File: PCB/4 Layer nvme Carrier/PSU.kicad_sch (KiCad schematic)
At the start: 176 parts, among them J481 Conn_01x02_Pin, J5 Barrel_Jack_Switch, J79 Conn_01x02_Pin, J80 Conn_01x02_Pin, J82 Conn_01x04, Q8 2N7002, SW1 SW_Push, SW2 SW_Push, U15 SY8253ADC, U16 SY8253ADC, U400 SY8253ADC, U410 SY8253ADC, U420 SY8253ADC, U430 SY8253ADC, U440 SY8253ADC, U450 SY8253ADC, U460 SY8253ADC, U470 SY8253ADC, U480 SY8253ADC, U78 AMS1117-3.3

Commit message: Prototyp_1
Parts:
- removed J481: Conn_01x02_Pin, Connector_PinHeader_2.54mm:PinHeader_1x02_P2.54mm_Vertical, symbol Connector:Conn_01x02_Pin
- added JP78: SolderJumper_2_Open, Jumper:SolderJumper-2_P1.3mm_Open_RoundedPad1.0x1.5mm, symbol Jumper:SolderJumper_2_Open
- C404, C414, C424, C434, C444, C454, C464, C474, C484, C72, C73: footprint Capacitor_SMD:C_0402_1005Metric -> A_HDJ_Library:C_0402_1005Metric
- C475, C476, C478, C479: MPN (none) -> CL10A226MP8NUNE
- C477: MPN (none) -> GRM155R71H104KE14D
- J79, J80, J82: now not fitted
- L471: MPN (none) -> WPN4020H2R2MT
- R50, R56: footprint Resistor_SMD:R_0402_1005Metric -> A_HDJ_Library:R_0402_1005Metric; MPN (none) -> RC0402FR-0710KL
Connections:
- net PWR_EN: now also JP78.1 (A)
- net at U480.4 (EN): now also JP78.2 (B)

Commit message: Silk and BOM changes
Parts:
- C401, C402, C405, C406, C408, C409, C411, C412, C415, C416, C418, C419, C421, C422, C425, C426, C428, C429, C431, C432, C435, C436, C438, C439, C441, C442, C445, C446, C448, C449, C451, C452, C455, C456, C458, C459, C461, C462, C465, C466, C468, C469, C475, C476, C478, C479, C481, C482, C485, C486, C488, C489, C64, C65, C67, C68, C74, C75, C76, C77, C80, C81, C82, C83, C91, C92: LCSC Part # (none) -> C86295; Package (none) -> 0603; Part# (none) -> C86295
- C403, C407, C413, C417, C423, C427, C433, C437, C443, C447, C453, C457, C463, C467, C477, C483, C487, C70, C71, C78, C79: LCSC Part # (none) -> C77020; Package (none) -> 0402; Part# (none) -> C77020
- C471, C472: LCSC Part # (none) -> C86295; MPN (none) -> CL10A226MP8NUNE; Package (none) -> 0603; Part# (none) -> C86295
- C473: LCSC Part # (none) -> C77020; MPN (none) -> GRM155R71H104KE14D; Package (none) -> 0402; Part# (none) -> C77020
- C66, C69: LCSC Part # (none) -> C29266; Package (none) -> 0402; Part# (none) -> C29266
- D21, D25: LCSC Part # (none) -> C521894; Package (none) -> 0402; Part# (none) -> C521894
- D22, D23: LCSC Part # (none) -> C434423; Package (none) -> 0603; Part# (none) -> C434423
- D24: LCSC Part # (none) -> C894530; MPN MMS3Z3B3GW -> SZMM3Z3V3T1G; MPN_alt (none) -> MMS3Z3B3GW; Package (none) -> SOD-323; Part# (none) -> C5674189
- D81: LCSC Part # (none) -> C553365; Package (none) -> SOD-128; Part# (none) -> C553365
- J5: LCSC Part # (none) -> C19189084; MPN DC007B-2.5-J -> HX DC007B-2.5-J; MPN_alt (none) -> DC007B-2.5-J; Package (none) -> Plugin; Part# (none) -> C17701686
- J79, J80: Package (none) -> Jumper; now fitted
- J82: LCSC Part # (none) -> C305819; Package (none) -> Plugin,P=5.08mm; Part# (none) -> C305819; now fitted
- JP78: Package (none) -> SolderJumper; now in the parts list
- L1, L2, L401, L411, L421, L431, L441, L451, L461, L471, L481: LCSC Part # (none) -> C98361; Package (none) -> SMD,4x4mm; Part# (none) -> C98361
- Q8: LCSC Part # (none) -> C7603342; Package (none) -> SOT-23; Part# (none) -> C7603342
- R401, R411, R421, R431, R441, R451, R461, R51, R59: LCSC Part # (none) -> C60491; Package (none) -> 0402; Part# (none) -> C60491
- R402, R412, R422, R432, R442, R452, R462, R60: LCSC Part # (none) -> C82868; Package (none) -> 0402; Part# (none) -> C82868
- R46, R48, R55: LCSC Part # (none) -> C106232; Package (none) -> 0402; Part# (none) -> C106232
- R47: LCSC Part # (none) -> C106235; Package (none) -> 0402; Part# (none) -> C106235
- R471: LCSC Part # (none) -> C60491; MPN (none) -> RC0402FR-07100KL; Package (none) -> 0402; Part# (none) -> C60491
- R472: LCSC Part # (none) -> C82868; MPN (none) -> RC0402FR-0722KL; Package (none) -> 0402; Part# (none) -> C82868
- R481, R57: LCSC Part # (none) -> C137935; Package (none) -> 0402; Part# (none) -> C137935
- R482, R49, R50, R56, R58: LCSC Part # (none) -> C60490; Package (none) -> 0402; Part# (none) -> C60490
- R52, R53: LCSC Part # (none) -> C114762; Package (none) -> 0402; Part# (none) -> C114762
- R54: LCSC Part # (none) -> C185442; Package (none) -> 0402; Part# (none) -> C185442
- SW1, SW2: LCSC Part # (none) -> C224978; MPN K2-1102SP-E3SC-04 -> DTSM-62K-V-T/R; MPN_alt (none) -> DTSMG-66K-V; Package (none) -> SMD; Part# (none) -> C2685894
- TP4, TP5, TP6: now not fitted
- U15, U16, U400, U410, U420, U430, U440, U450, U460, U480: LCSC Part # (none) -> C93736; Package (none) -> SOT-23-6; Part# (none) -> C93736
- U470: LCSC Part # (none) -> C93736; MPN (none) -> SY8253ADC; Package (none) -> SOT-23-6; Part# (none) -> C93736
- U78: LCSC Part # (none) -> C347222; Package (none) -> SOT-223; Part# (none) -> C347222

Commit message: Fix USB3.2. And Updated some C
Fix USB3.2 Error (twisted Tx and Rx). And Updated some C from 22uF/10V to 22uF/16V
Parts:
- C401, C402, C411, C412, C421, C422, C431, C432, C441, C442, C451, C452, C461, C462, C481, C482, C64, C65, C67, C68, C92: value 22uF/10V -> 22uF/16V; LCSC Part # C86295 -> C2762594; MPN CL10A226MP8NUNE -> CL10A226MO7JZNC
- C471, C472: value 22uF/10V -> 22uF/16V

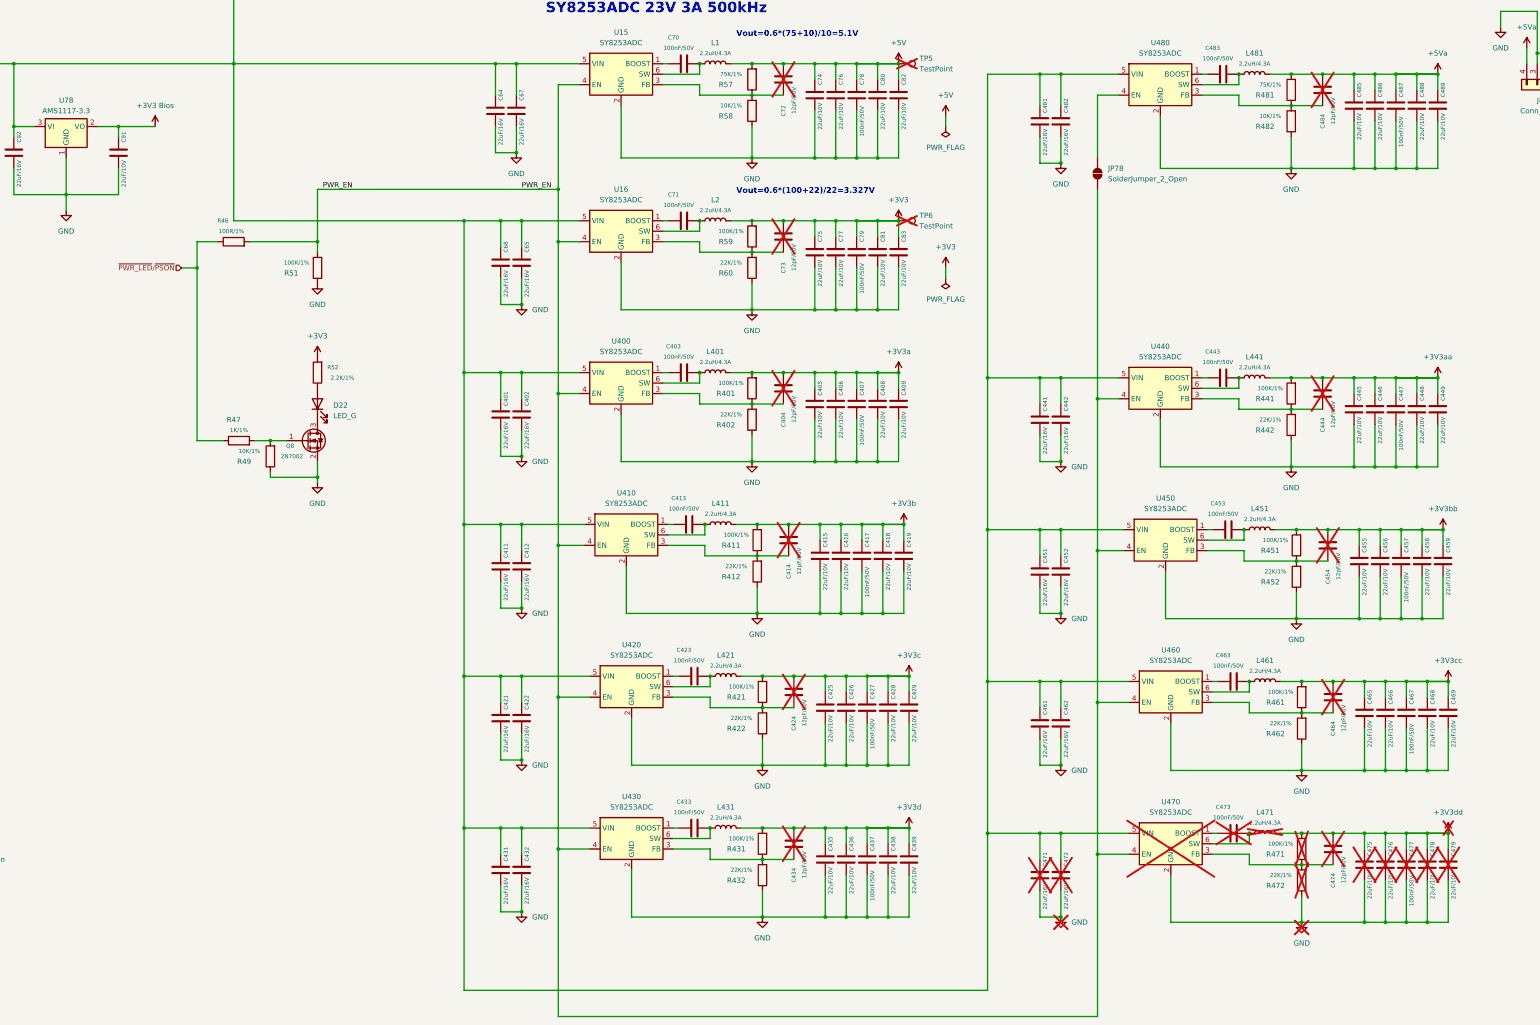
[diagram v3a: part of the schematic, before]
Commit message: new JPG, new 3V3 names and del the M.2 60mm mounts
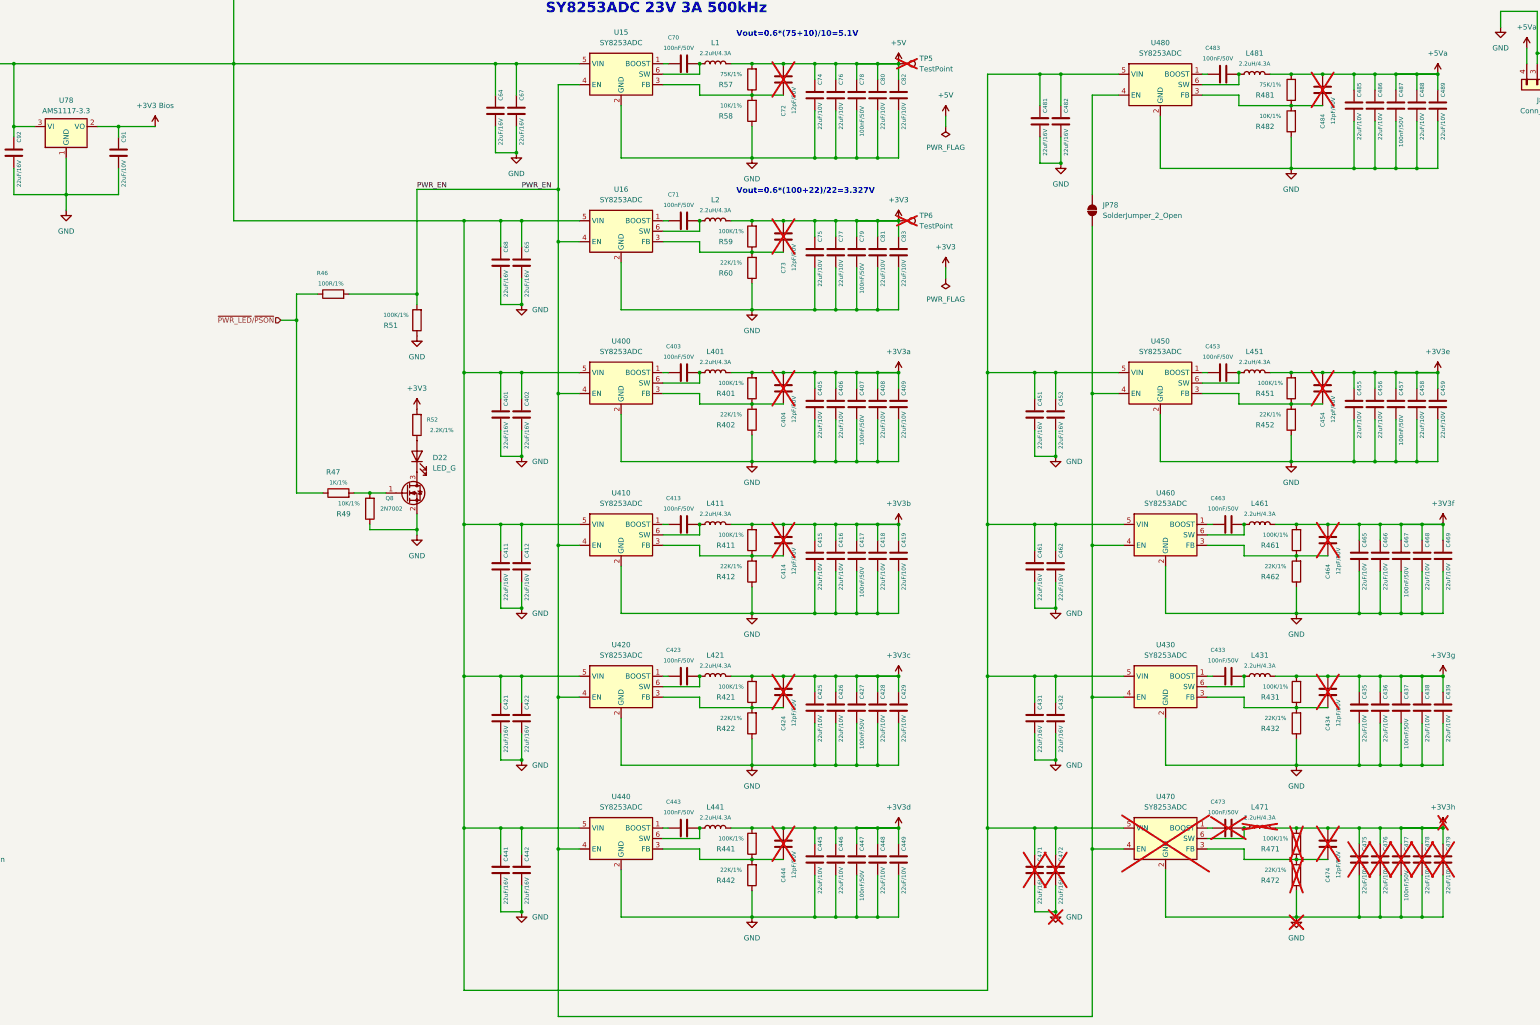
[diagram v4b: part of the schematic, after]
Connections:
- net +3V3aa is gone; now on net +3V3d: C444.1, C445.2, C446.2, C447.1, C448.2, C449.2, L441.2, R441.2
- net +3V3d: no longer C434.1, C435.2, C436.2, C437.1, C438.2, C439.2, L431.2, R431.2
- net +3V3bb renamed +3V3e
- net +3V3cc renamed +3V3f
- net +3V3dd renamed +3V3h
- new net +3V3g: C434.1, C435.2, C436.2, C437.1, C438.2, C439.2, L431.2, R431.2
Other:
- moved on the sheet: C413, C414, C415, C416, C417, C418, C419, C423, C424, C425, C426, C427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
